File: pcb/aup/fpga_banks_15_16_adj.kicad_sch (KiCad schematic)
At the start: 1 part, among them U1 XC7A50T-2FGG484C

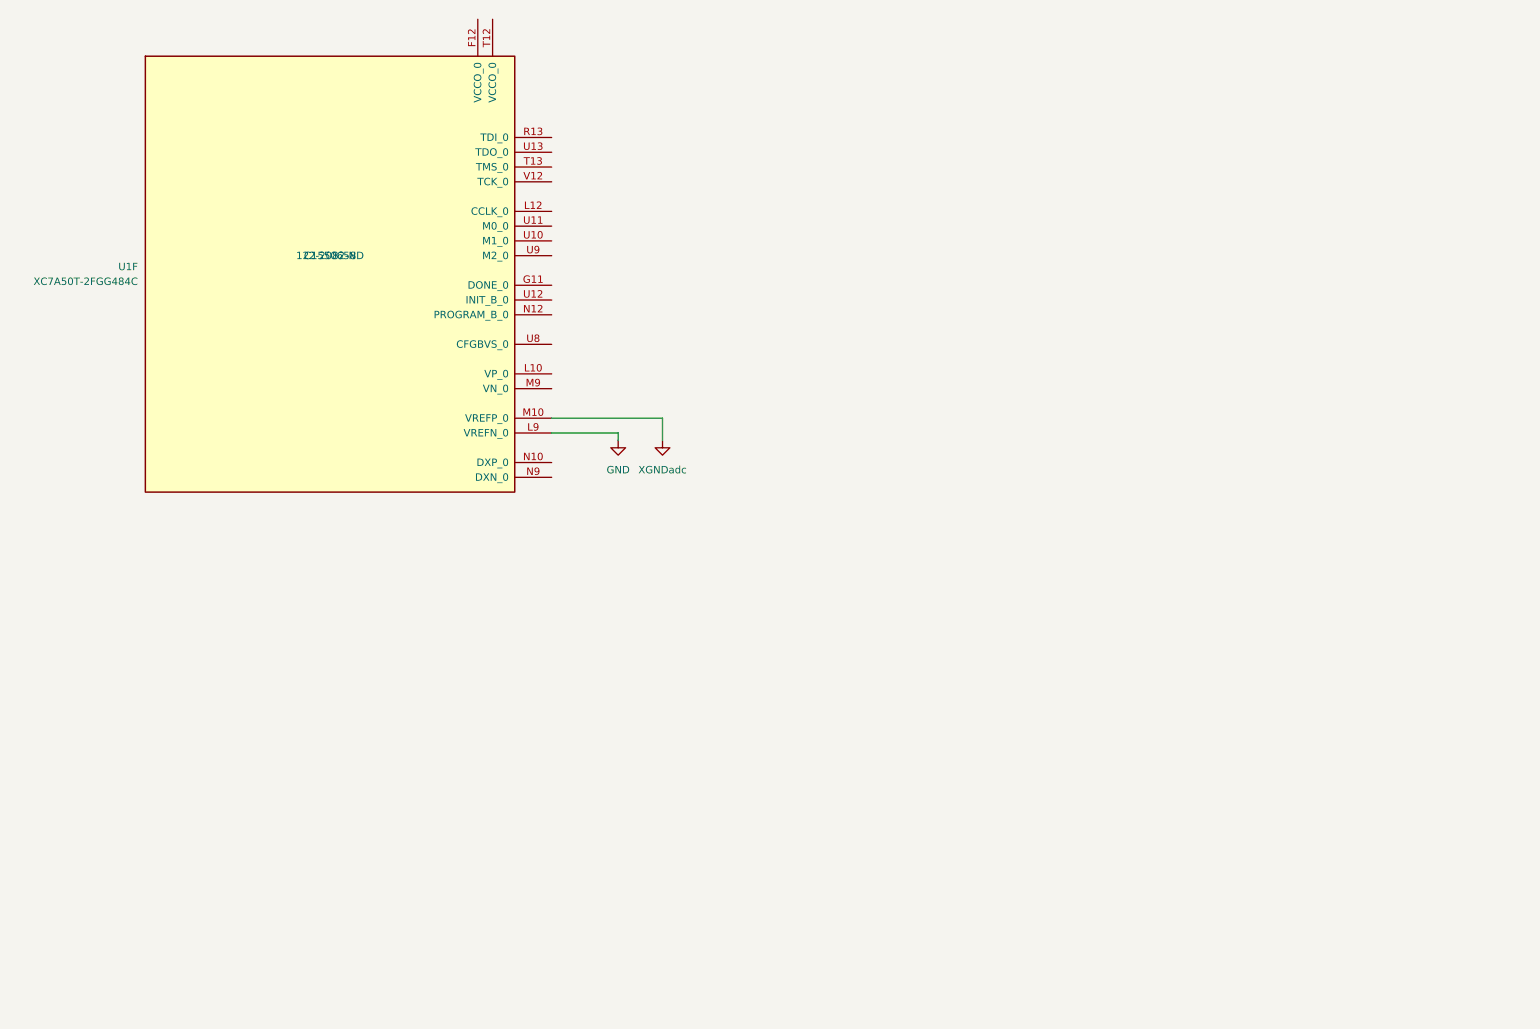
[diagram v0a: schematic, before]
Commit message: Add hierarchical sheets for banks and add caps.
There are some stale sheets in this commit, but I don't want to delete
an active one accidentally. Save them all for now, and then go back and
clean them up.
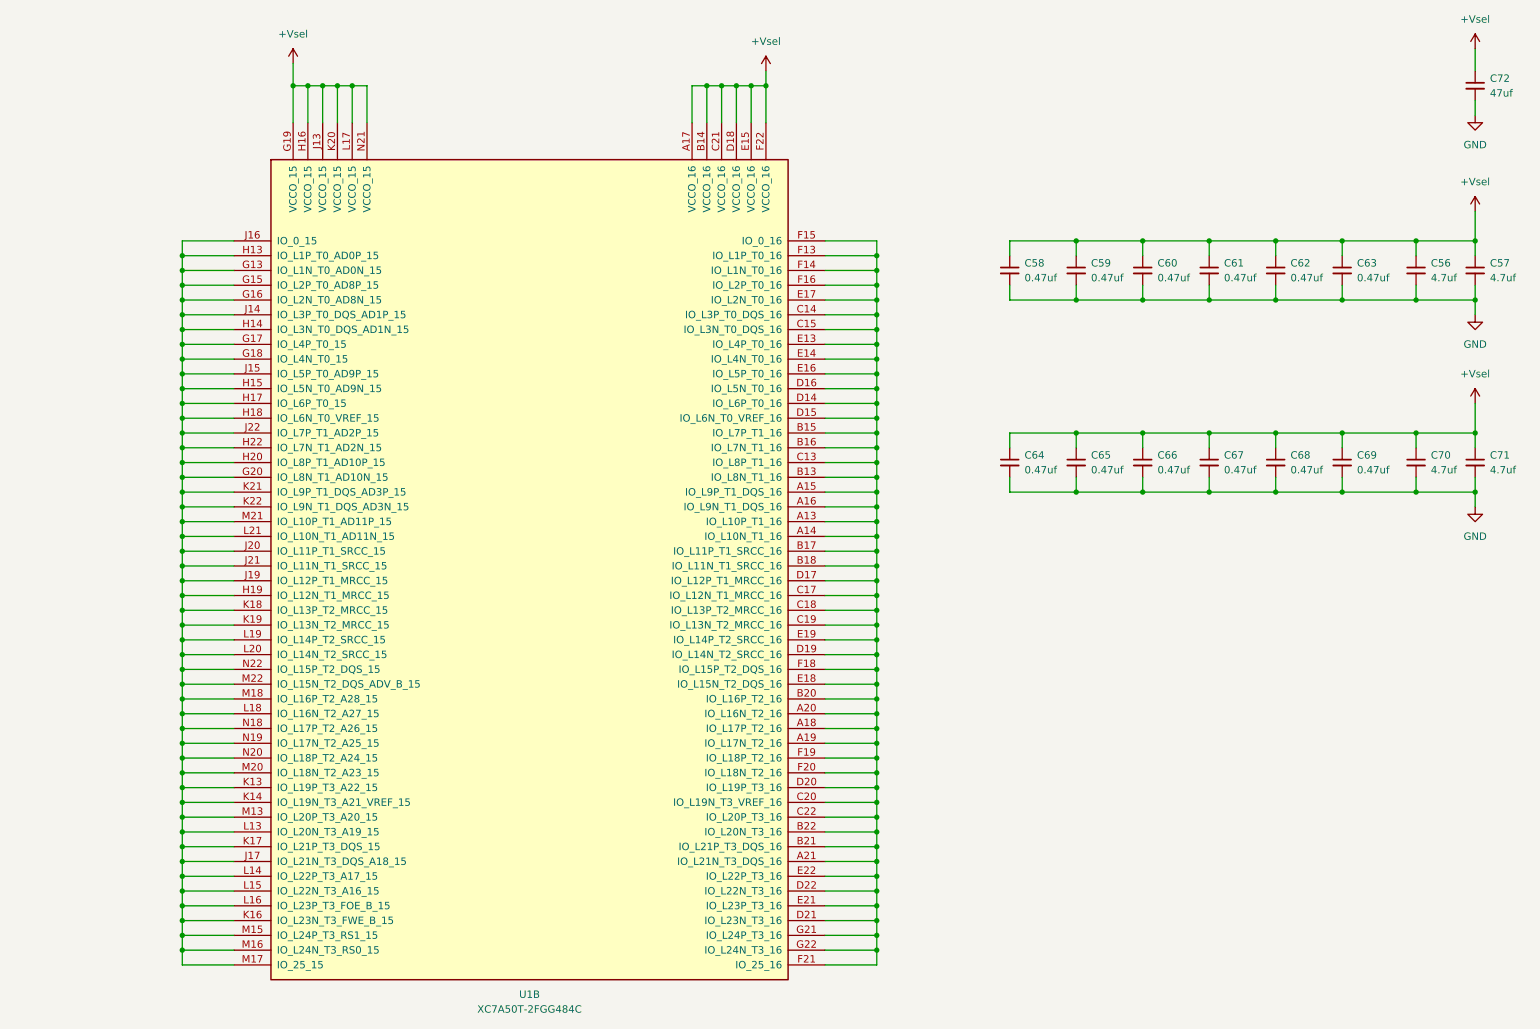
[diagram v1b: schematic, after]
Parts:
- removed U1: XC7A50T-2FGG484C, !Xilinx:Xilinx_FGG484, symbol !Xilinx:XC7A50T-FGG484
- added C56, C57, C70, C71: 4.7uf, Capacitor_SMD:C_0805_2012Metric, symbol !Misc:C_4.7uf_0805
- added C58, C59, C60, C61, C62, C63, C64, C65, C66, C67, C68, C69: 0.47uf, Capacitor_SMD:C_0402_1005Metric, symbol !Misc:C_0.47uf_0402
- added C72: 47uf, Capacitor_SMD:C_1206_3216Metric, symbol !Misc:C_47uf_1206
- added U1: XC7A50T-2FGG484C, !Xilinx:Xilinx_FGG484, symbol !Xilinx:XC7A50T-FGG484
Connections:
- net GND: now also C56.2, C57.2, C58.2, C59.2, C60.2, C61.2, C62.2, C63.2, C64.2, C65.2, C66.2, C67.2, C68.2, C69.2, C70.2, C71.2, C72.2
- new net: U1.A13 (IO_L10P_T1_16), U1.A14 (IO_L10N_T1_16), U1.A15 (IO_L9P_T1_DQS_16), U1.A16 (IO_L9N_T1_DQS_16), U1.A18 (IO_L17P_T2_16), U1.A19 (IO_L17N_T2_16), U1.A20 (IO_L16N_T2_16), U1.A21 (IO_L21N_T3_DQS_16), U1.B13 (IO_L8N_T1_16), U1.B15 (IO_L7P_T1_16), U1.B16 (IO_L7N_T1_16), U1.B17 (IO_L11P_T1_SRCC_16), U1.B18 (IO_L11N_T1_SRCC_16), U1.B20 (IO_L16P_T2_16), U1.B21 (IO_L21P_T3_DQS_16), U1.B22 (IO_L20N_T3_16), U1.C13 (IO_L8P_T1_16), U1.C14 (IO_L3P_T0_DQS_16), U1.C15 (IO_L3N_T0_DQS_16), U1.C17 (IO_L12N_T1_MRCC_16), U1.C18 (IO_L13P_T2_MRCC_16), U1.C19 (IO_L13N_T2_MRCC_16), U1.C20 (IO_L19N_T3_VREF_16), U1.C22 (IO_L20P_T3_16), U1.D14 (IO_L6P_T0_16), U1.D15 (IO_L6N_T0_VREF_16), U1.D16 (IO_L5N_T0_16), U1.D17 (IO_L12P_T1_MRCC_16), U1.D19 (IO_L14N_T2_SRCC_16), U1.D20 (IO_L19P_T3_16), U1.D21 (IO_L23N_T3_16), U1.D22 (IO_L22N_T3_16), U1.E13 (IO_L4P_T0_16), U1.E14 (IO_L4N_T0_16), U1.E16 (IO_L5P_T0_16), U1.E17 (IO_L2N_T0_16), U1.E18 (IO_L15N_T2_DQS_16), U1.E19 (IO_L14P_T2_SRCC_16), U1.E21 (IO_L23P_T3_16), U1.E22 (IO_L22P_T3_16), U1.F13 (IO_L1P_T0_16), U1.F14 (IO_L1N_T0_16), U1.F15 (IO_0_16), U1.F16 (IO_L2P_T0_16), U1.F18 (IO_L15P_T2_DQS_16), U1.F19 (IO_L18P_T2_16), U1.F20 (IO_L18N_T2_16), U1.F21 (IO_25_16), U1.G21 (IO_L24P_T3_16), U1.G22 (IO_L24N_T3_16)
- new net: U1.G13 (IO_L1N_T0_AD0N_15), U1.G15 (IO_L2P_T0_AD8P_15), U1.G16 (IO_L2N_T0_AD8N_15), U1.G17 (IO_L4P_T0_15), U1.G18 (IO_L4N_T0_15), U1.G20 (IO_L8N_T1_AD10N_15), U1.H13 (IO_L1P_T0_AD0P_15), U1.H14 (IO_L3N_T0_DQS_AD1N_15), U1.H15 (IO_L5N_T0_AD9N_15), U1.H17 (IO_L6P_T0_15), U1.H18 (IO_L6N_T0_VREF_15), U1.H19 (IO_L12N_T1_MRCC_15), U1.H20 (IO_L8P_T1_AD10P_15), U1.H22 (IO_L7N_T1_AD2N_15), U1.J14 (IO_L3P_T0_DQS_AD1P_15), U1.J15 (IO_L5P_T0_AD9P_15), U1.J16 (IO_0_15), U1.J17 (IO_L21N_T3_DQS_A18_15), U1.J19 (IO_L12P_T1_MRCC_15), U1.J20 (IO_L11P_T1_SRCC_15), U1.J21 (IO_L11N_T1_SRCC_15), U1.J22 (IO_L7P_T1_AD2P_15), U1.K13 (IO_L19P_T3_A22_15), U1.K14 (IO_L19N_T3_A21_VREF_15), U1.K16 (IO_L23N_T3_FWE_B_15), U1.K17 (IO_L21P_T3_DQS_15), U1.K18 (IO_L13P_T2_MRCC_15), U1.K19 (IO_L13N_T2_MRCC_15), U1.K21 (IO_L9P_T1_DQS_AD3P_15), U1.K22 (IO_L9N_T1_DQS_AD3N_15), U1.L13 (IO_L20N_T3_A19_15), U1.L14 (IO_L22P_T3_A17_15), U1.L15 (IO_L22N_T3_A16_15), U1.L16 (IO_L23P_T3_FOE_B_15), U1.L18 (IO_L16N_T2_A27_15), U1.L19 (IO_L14P_T2_SRCC_15), U1.L20 (IO_L14N_T2_SRCC_15), U1.L21 (IO_L10N_T1_AD11N_15), U1.M13 (IO_L20P_T3_A20_15), U1.M15 (IO_L24P_T3_RS1_15), U1.M16 (IO_L24N_T3_RS0_15), U1.M17 (IO_25_15), U1.M18 (IO_L16P_T2_A28_15), U1.M20 (IO_L18N_T2_A23_15), U1.M21 (IO_L10P_T1_AD11P_15), U1.M22 (IO_L15N_T2_DQS_ADV_B_15), U1.N18 (IO_L17P_T2_A26_15), U1.N19 (IO_L17N_T2_A25_15), U1.N20 (IO_L18P_T2_A24_15), U1.N22 (IO_L15P_T2_DQS_15)
- new net +Vsel: C56.1, C57.1, C58.1, C59.1, C60.1, C61.1, C62.1, C63.1, C64.1, C65.1, C66.1, C67.1, C68.1, C69.1, C70.1, C71.1, C72.1, U1.A17 (VCCO_16), U1.B14 (VCCO_16), U1.C21 (VCCO_16), U1.D18 (VCCO_16), U1.E15 (VCCO_16), U1.F22 (VCCO_16), U1.G19 (VCCO_15), U1.H16 (VCCO_15), U1.J13 (VCCO_15), U1.K20 (VCCO_15), U1.L17 (VCCO_15), U1.N21 (VCCO_15)

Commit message: Switch 0.47uf caps under bga to 0201
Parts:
- C58, C59, C60, C61, C62, C63, C64, C65, C66, C67, C68, C69: footprint Capacitor_SMD:C_0402_1005Metric -> Capacitor_SMD:C_0201_0603Metric; symbol !Misc:C_0.47uf_0402 -> !Misc:C_0.47uf_0201; Digi-Key Part Number 1276-1173-1-ND -> 1276-1337-1-ND; LCSC Part # C1779 -> C318543
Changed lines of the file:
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@@
 		(polyline
 			(pts
-				(xy 48.26 59.69) (xy 48.26 189.23) (xy 50.8 189.23) (xy 50.8 59.69)
+				(xy 157.48 59.69) (xy 157.48 189.23) (xy 160.02 189.23) (xy 160.02 59.69)
 			)
 			(stroke
@@
 		(polyline
 			(pts
-				(xy 157.48 59.69) (xy 157.48 189.23) (xy 160.02 189.23) (xy 160.02 59.69)
+				(xy 48.26 59.69) (xy 48.26 189.23) (xy 50.8 189.23) (xy 50.8 59.69)
 			)
 			(stroke
@@
 	)
 	(symbol
-		(lib_id "!Misc:C_0.47uf_0402")
+		(lib_id "!Misc:C_0.47uf_0201")
 		(at 210.82 66.04 0)
 		(unit 1)
@@
 			)
 		)
-		(property "Footprint" "Capacitor_SMD:C_0402_1005Metric"
+		(property "Footprint" "Capacitor_SMD:C_0201_0603Metric"
 			(at 210.82 66.04 0)
 			(effects
@@
 			)
 		)
-		(property "Description" "Unpolarized capacitor 0.47uf 0402"
+		(property "Description" "Unpolarized capacitor 0.47uf 0201"
 			(at 210.82 66.04 0)
 			(effects
@@
 			)
 		)
-		(property "LCSC Part #" "C1779"
+		(property "LCSC Part #" "C318543"
 			(at 210.82 66.04 0)
 			(effects
@@
 			)
 		)
-		(property "Digi-Key Part Number" "1276-1173-1-ND"
+		(property "Digi-Key Part Number" "1276-1337-1-ND"
 			(at 210.82 66.04 0)
 			(effects
@@
 	)
 	(symbol
-		(lib_id "!Misc:C_0.47uf_0402")
+		(lib_id "!Misc:C_0.47uf_0201")
 		(at 199.39 66.04 0)
 		(unit 1)
@@
 			)
 		)
-		(property "Footprint" "Capacitor_SMD:C_0402_1005Metric"
+		(property "Footprint" "Capacitor_SMD:C_0201_0603Metric"
 			(at 199.39 66.04 0)
 			(effects
@@
 			)
 		)
-		(property "Description" "Unpolarized capacitor 0.47uf 0402"
+		(property "Description" "Unpolarized capacitor 0.47uf 0201"
 			(at 199.39 66.04 0)
 			(effects
@@
 			)
 		)
-		(property "LCSC Part #" "C1779"
+		(property "LCSC Part #" "C318543"
 			(at 199.39 66.04 0)
 			(effects
@@
 			)
 		)
-		(property "Digi-Key Part Number" "1276-1173-1-ND"
+		(property "Digi-Key Part Number" "1276-1337-1-ND"
 			(at 199.39 66.04 0)
 			(effects
@@
 	)
 	(symbol
-		(lib_id "!Misc:C_0.47uf_0402")
+		(lib_id "!Misc:C_0.47uf_0201")
 		(at 233.68 66.04 0)
 		(unit 1)
@@
 			)
 		)
-		(property "Footprint" "Capacitor_SMD:C_0402_1005Metric"
+		(property "Footprint" "Capacitor_SMD:C_0201_0603Metric"
 			(at 233.68 66.04 0)
 			(effects
@@
 			)
 		)
-		(property "Description" "Unpolarized capacitor 0.47uf 0402"
+		(property "Description" "Unpolarized capacitor 0.47uf 0201"
 			(at 233.68 66.04 0)
 			(effects
@@
 			)
 		)
-		(property "LCSC Part #" "C1779"
+		(property "LCSC Part #" "C318543"
 			(at 233.68 66.04 0)
 			(effects
@@
 			)
 		)
-		(property "Digi-Key Part Number" "1276-1173-1-ND"
+		(property "Digi-Key Part Number" "1276-1337-1-ND"
 			(at 233.68 66.04 0)
 			(effects
@@
 	)
 	(symbol
-		(lib_id "!Misc:C_0.47uf_0402")
+		(lib_id "!Misc:C_0.47uf_0201")
 		(at 245.11 66.04 0)
 		(unit 1)
@@
 			)
 		)
-		(property "Footprint" "Capacitor_SMD:C_0402_1005Metric"
+		(property "Footprint" "Capacitor_SMD:C_0201_0603Metric"
 			(at 245.11 66.04 0)
 			(effects
@@
 			)
 		)
-		(property "Description" "Unpolarized capacitor 0.47uf 0402"
+		(property "Description" "Unpolarized capacitor 0.47uf 0201"
 			(at 245.11 66.04 0)
 			(effects
@@
 			)
 		)
-		(property "LCSC Part #" "C1779"
+		(property "LCSC Part #" "C318543"
 			(at 245.11 66.04 0)
 			(effects
@@
 			)
 		)
-		(property "Digi-Key Part Number" "1276-1173-1-ND"
+		(property "Digi-Key Part Number" "1276-1337-1-ND"
 			(at 245.11 66.04 0)
 			(effects
@@
 	)
 	(symbol
-		(lib_id "!Misc:C_0.47uf_0402")
+		(lib_id "!Misc:C_0.47uf_0201")
 		(at 233.68 99.06 0)
 		(unit 1)
@@
 			)
 		)
-		(property "Footprint" "Capacitor_SMD:C_0402_1005Metric"
+		(property "Footprint" "Capacitor_SMD:C_0201_0603Metric"
 			(at 233.68 99.06 0)
 			(effects
@@
 			)
 		)
-		(property "Description" "Unpolarized capacitor 0.47uf 0402"
+		(property "Description" "Unpolarized capacitor 0.47uf 0201"
 			(at 233.68 99.06 0)
 			(effects
@@
 			)
 		)
-		(property "LCSC Part #" "C1779"
+		(property "LCSC Part #" "C318543"
 			(at 233.68 99.06 0)
 			(effects
@@
 			)
 		)
-		(property "Digi-Key Part Number" "1276-1173-1-ND"
+		(property "Digi-Key Part Number" "1276-1337-1-ND"
 			(at 233.68 99.06 0)
 			(effects
@@
 	)
 	(symbol
-		(lib_id "!Misc:C_0.47uf_0402")
+		(lib_id "!Misc:C_0.47uf_0201")
 		(at 222.25 66.04 0)
 		(unit 1)
@@
 			)
 		)
-		(property "Footprint" "Capacitor_SMD:C_0402_1005Metric"
+		(property "Footprint" "Capacitor_SMD:C_0201_0603Metric"
 			(at 222.25 66.04 0)
 			(effects
@@
 			)
 		)
-		(property "Description" "Unpolarized capacitor 0.47uf 0402"
+		(property "Description" "Unpolarized capacitor 0.47uf 0201"
 			(at 222.25 66.04 0)
 			(effects
@@
 			)
 		)
-		(property "LCSC Part #" "C1779"
+		(property "LCSC Part #" "C318543"
 			(at 222.25 66.04 0)
 			(effects
@@
 			)
 		)
-		(property "Digi-Key Part Number" "1276-1173-1-ND"
+		(property "Digi-Key Part Number" "1276-1337-1-ND"
 			(at 222.25 66.04 0)
 			(effects
@@
 	)
 	(symbol
-		(lib_id "!Misc:C_0.47uf_0402")
+		(lib_id "!Misc:C_0.47uf_0201")
 		(at 187.96 66.04 0)
 		(unit 1)
@@
 			)
 		)
-		(property "Footprint" "Capacitor_SMD:C_0402_1005Metric"
+		(property "Footprint" "Capacitor_SMD:C_0201_0603Metric"
 			(at 187.96 66.04 0)
 			(effects
@@
 			)
 		)
-		(property "Description" "Unpolarized capacitor 0.47uf 0402"
+		(property "Description" "Unpolarized capacitor 0.47uf 0201"
 			(at 187.96 66.04 0)
 			(effects
@@
 			)
 		)
-		(property "LCSC Part #" "C1779"
+		(property "LCSC Part #" "C318543"
 			(at 187.96 66.04 0)
 			(effects
@@
 			)
 		)
-		(property "Digi-Key Part Number" "1276-1173-1-ND"
+		(property "Digi-Key Part Number" "1276-1337-1-ND"
 			(at 187.96 66.04 0)
 			(effects
@@
 	)
 	(symbol
-		(lib_id "!Misc:C_0.47uf_0402")
+		(lib_id "!Misc:C_0.47uf_0201")
 		(at 199.39 99.06 0)
 		(unit 1)
@@
 			)
 		)
-		(property "Footprint" "Capacitor_SMD:C_0402_1005Metric"
+		(property "Footprint" "Capacitor_SMD:C_0201_0603Metric"
 			(at 199.39 99.06 0)
 			(effects
@@
 			)
 		)
-		(property "Description" "Unpolarized capacitor 0.47uf 0402"
+		(property "Description" "Unpolarized capacitor 0.47uf 0201"
 			(at 199.39 99.06 0)
 			(effects
@@
 			)
 		)
-		(property "LCSC Part #" "C1779"
+		(property "LCSC Part #" "C318543"
 			(at 199.39 99.06 0)
 			(effects
@@
 			)
 		)
-		(property "Digi-Key Part Number" "1276-1173-1-ND"
+		(property "Digi-Key Part Number" "1276-1337-1-ND"
 			(at 199.39 99.06 0)
 			(effects
@@
 	)
 	(symbol
-		(lib_id "!Misc:C_0.47uf_0402")
+		(lib_id "!Misc:C_0.47uf_0201")
 		(at 187.96 99.06 0)
 		(unit 1)
@@
 			)
 		)
-		(property "Footprint" "Capacitor_SMD:C_0402_1005Metric"
+		(property "Footprint" "Capacitor_SMD:C_0201_0603Metric"
 			(at 187.96 99.06 0)
 			(effects
@@
 			)
 		)
-		(property "Description" "Unpolarized capacitor 0.47uf 0402"
+		(property "Description" "Unpolarized capacitor 0.47uf 0201"
 			(at 187.96 99.06 0)
 			(effects
@@
 			)
 		)
-		(property "LCSC Part #" "C1779"
+		(property "LCSC Part #" "C318543"
 			(at 187.96 99.06 0)
 			(effects
@@
 			)
 		)
-		(property "Digi-Key Part Number" "1276-1173-1-ND"
+		(property "Digi-Key Part Number" "1276-1337-1-ND"
 			(at 187.96 99.06 0)
 			(effects
@@
 	)
 	(symbol
-		(lib_id "!Misc:C_0.47uf_0402")
+		(lib_id "!Misc:C_0.47uf_0201")
 		(at 245.11 99.06 0)
 		(unit 1)
@@
 			)
 		)
-		(property "Footprint" "Capacitor_SMD:C_0402_1005Metric"
+		(property "Footprint" "Capacitor_SMD:C_0201_0603Metric"
 			(at 245.11 99.06 0)
 			(effects
@@
 			)
 		)
-		(property "Description" "Unpolarized capacitor 0.47uf 0402"
+		(property "Description" "Unpolarized capacitor 0.47uf 0201"
 			(at 245.11 99.06 0)
 			(effects
@@
 			)
 		)
-		(property "LCSC Part #" "C1779"
+		(property "LCSC Part #" "C318543"
 			(at 245.11 99.06 0)
 			(effects
@@
 			)
 		)
-		(property "Digi-Key Part Number" "1276-1173-1-ND"
+		(property "Digi-Key Part Number" "1276-1337-1-ND"
 			(at 245.11 99.06 0)
 			(effects
@@
 	)
 	(symbol
-		(lib_id "!Misc:C_0.47uf_0402")
+		(lib_id "!Misc:C_0.47uf_0201")
 		(at 222.25 99.06 0)
 		(unit 1)
@@
 			)
 		)
-		(property "Footprint" "Capacitor_SMD:C_0402_1005Metric"
+		(property "Footprint" "Capacitor_SMD:C_0201_0603Metric"
 			(at 222.25 99.06 0)
 			(effects
@@
 			)
 		)
-		(property "Description" "Unpolarized capacitor 0.47uf 0402"
+		(property "Description" "Unpolarized capacitor 0.47uf 0201"
 			(at 222.25 99.06 0)
 			(effects
@@
 			)
 		)
-		(property "LCSC Part #" "C1779"
+		(property "LCSC Part #" "C318543"
 			(at 222.25 99.06 0)
 			(effects
@@
 			)
 		)
-		(property "Digi-Key Part Number" "1276-1173-1-ND"
+		(property "Digi-Key Part Number" "1276-1337-1-ND"
 			(at 222.25 99.06 0)
 			(effects
@@
 	)
 	(symbol
-		(lib_id "!Misc:C_0.47uf_0402")
+		(lib_id "!Misc:C_0.47uf_0201")
 		(at 210.82 99.06 0)
 		(unit 1)
@@
 			)
 		)
-		(property "Footprint" "Capacitor_SMD:C_0402_1005Metric"
+		(property "Footprint" "Capacitor_SMD:C_0201_0603Metric"
 			(at 210.82 99.06 0)
 			(effects
@@
 			)
 		)
-		(property "Description" "Unpolarized capacitor 0.47uf 0402"
+		(property "Description" "Unpolarized capacitor 0.47uf 0201"
 			(at 210.82 99.06 0)
 			(effects
@@
 			)
 		)
-		(property "LCSC Part #" "C1779"
+		(property "LCSC Part #" "C318543"
 			(at 210.82 99.06 0)
 			(effects
@@
 			)
 		)
-		(property "Digi-Key Part Number" "1276-1173-1-ND"
+		(property "Digi-Key Part Number" "1276-1337-1-ND"
 			(at 210.82 99.06 0)
 			(effects
